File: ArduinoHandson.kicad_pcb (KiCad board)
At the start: 2 copper layers, 33 x 64.4 mm, 19 parts, among them IC1 ATMEGA328-P, P2 USB micro, P3 Power, P4 Digital2, P5 Analog, P6 Digital1, SW1 SW_PUSH, U1 FT232RL, X1 CRYSTAL

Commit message: 配線のみ
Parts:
- turned U1 to 270 degrees
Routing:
- net GND: track 0.00 -> 149.0 mm, vias 0 -> 5
- net +5V: track 0.00 -> 88.4 mm
- net /D13: track 0.00 -> 59.8 mm
- net /D1: track 0.00 -> 36.6 mm
- net /Reset: track 0.00 -> 35.7 mm
- net /D0: track 0.00 -> 34.2 mm
- net +3V3: track 0.00 -> 31.9 mm, vias 0 -> 3
- net /D2: track 0.00 -> 22.7 mm
- net /D4: track 0.00 -> 22.4 mm
- net /D3: track 0.00 -> 22.0 mm
- net Net-(D2-Pad1): track 0.00 -> 19.4 mm, vias 0 -> 1
- net /D8: track 0.00 -> 19.0 mm
- net Net-(D1-Pad1): track 0.00 -> 13.3 mm
- net /D5: track 0.00 -> 12.5 mm
- net /D6: track 0.00 -> 12.5 mm
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
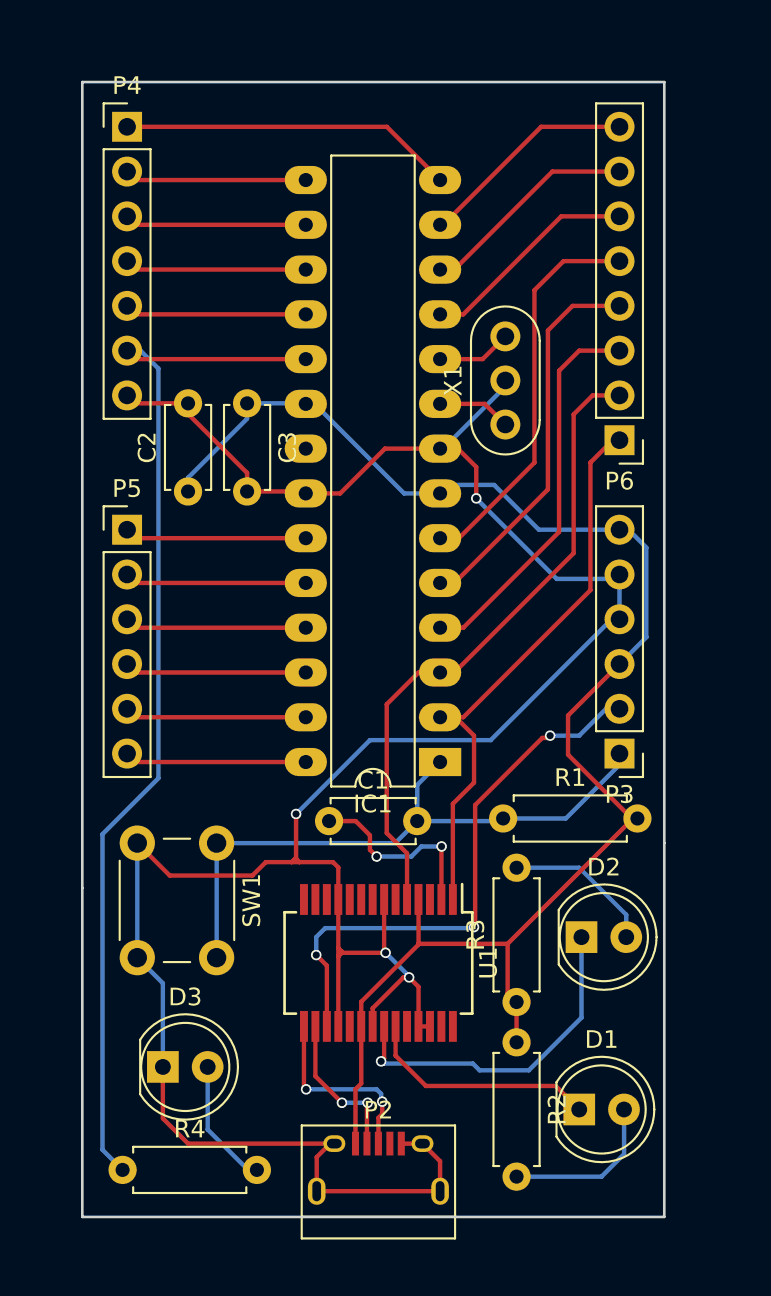
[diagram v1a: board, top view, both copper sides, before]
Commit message: 外形変更、文字表示対応
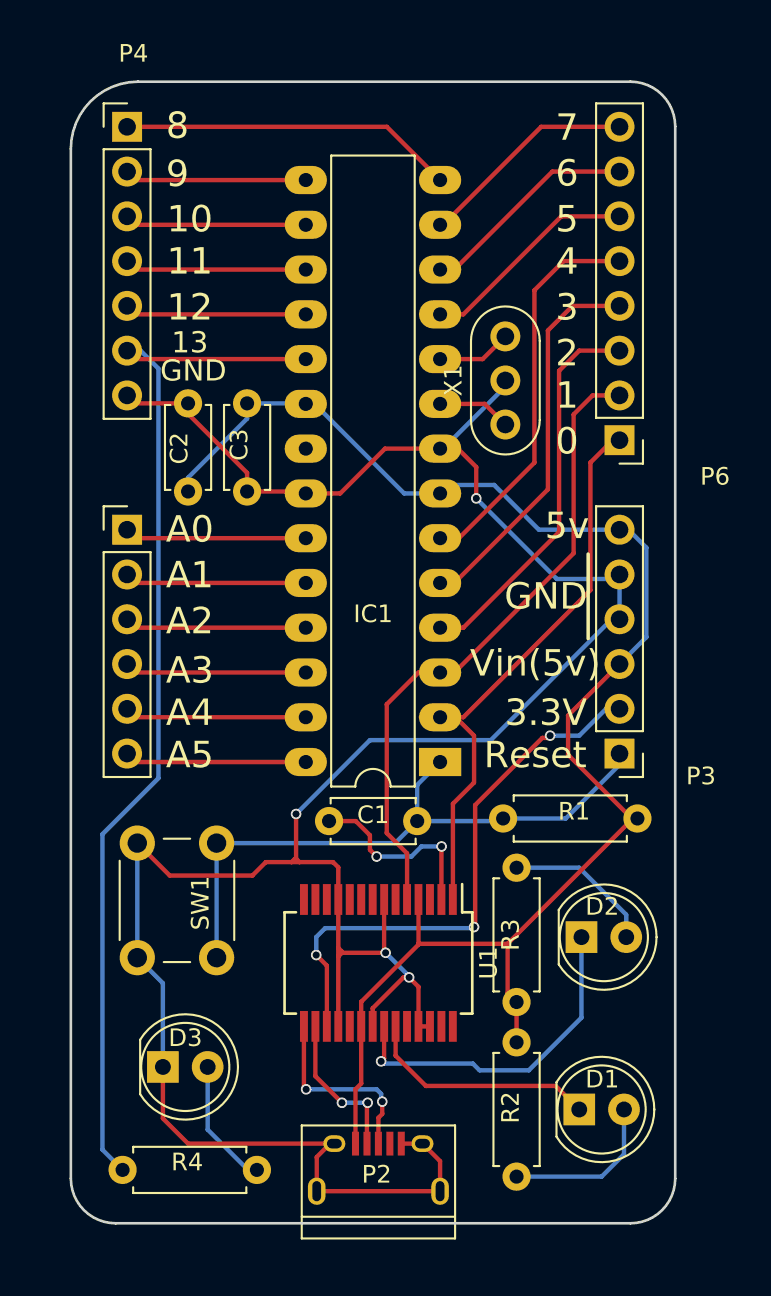
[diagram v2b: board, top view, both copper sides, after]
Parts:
- SW1: value SW_PUSH -> Reset
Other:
- board size 33 x 64.4 mm -> 34.3 x 64.8 mm
- board text added: "0"
- board text added: "1"
- board text added: "10"
- board text added: "11"
- board text added: "12"
- board text added: "13"
- board text added: "2"
- board text added: "3"
- board text added: "3.3V"
- board text added: "4"
- board text added: "5"
- board text added: "5v"
- board text added: "6"
- board text added: "7"
- board text added: "8"
- board text added: "9"
- board text added: "A0"
- board text added: "A1"
- board text added: "A2"
- board text added: "A3"
- board text added: "A4"
- board text added: "A5"
- board text added: "GND"
- board text added: "Reset"
- board text added: "Vin(5v)"

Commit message: ベタグランド
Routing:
- added copper zone on B.Cu, net GND
- added copper zone on F.Cu, net GND

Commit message: 回路図+配線図完成
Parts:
- removed the P2 at (54.9, 94.6)
- added P1: USB_B, Connect:USB_B_MUSB_Straight, F.Cu at (56.2, 90.6)
- SW1: value Reset -> SW_PUSH
- moved R1 24.3 mm to (38.9, 82.4)
- moved D3 23.8 mm to (66.0, 93.8)
- moved R3 16.6 mm to (46.5, 88.8), turned to 180 degrees
- moved R2 16.3 mm to (46.5, 85.6), turned to 180 degrees
- moved D1 11.5 mm to (66.0, 79.8)
- moved R4 6.70 mm to (46.5, 92.0), turned to 180 degrees
- moved SW1 5.72 mm to (40.2, 74.7), turned to 0 degrees
- moved D2 5.28 mm to (66.0, 86.8)
- moved U1 1.33 mm to (54.6, 81.7)
- renumbered P3 to P2, P4 to P3, P5 to P4, P6 to P5
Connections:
- IC1 pad 21: Net-(IC1-Pad21) -> +5V
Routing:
- net Net-(D1-Pad2): track 9.16 -> 34.9 mm
- net Net-(D3-Pad2): track 7.30 -> 32.4 mm
- net Net-(D2-Pad2): track 8.60 -> 31.6 mm
- net GND: track 149.0 -> 129.8 mm, vias 5 -> 3
- net +5V: track 88.4 -> 96.3 mm, vias 0 -> 1
- net /Reset: track 35.7 -> 42.1 mm
- net Net-(D2-Pad1): track 19.4 -> 13.9 mm, vias 1 -> 0
- net Net-(C1-Pad1): track 11.0 -> 8.60 mm, vias 2 -> 1
- net /D-: track 8.75 -> 6.41 mm, vias 2 -> 0
- net Net-(D1-Pad1): track 13.3 -> 15.6 mm
- net +3V3: track 31.9 -> 29.9 mm, vias 3 -> 2
- net /D0: track 34.2 -> 35.8 mm
- net /D+: track 10.9 -> 9.43 mm, vias 2 -> 0
- net /D1: track 36.6 -> 35.3 mm
- net /D13: track 59.8 -> 59.0 mm, vias 0 -> 1
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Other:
- board size 34.3 x 64.8 mm -> 35 x 66 mm
- net class Power added: clearance 0.2, trace_width 0.4, via_dia 0.6, via_drill 0.4

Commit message: 配線図開始
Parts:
- removed D3: 13LED, LEDs:LED_D5.0mm
- removed R4: 500, Resistors_ThroughHole:R_Axial_DIN0207_L6.3mm_D2.5mm_P7.62mm_Horizontal
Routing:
- net /D13: track 59.0 -> 11.7 mm, vias 1 -> 0
- net Net-(D3-Pad2): track 32.4 -> 0.00 mm
- net /A5: track 10.3 -> 0.68 mm
- net /A4: track 10.3 -> 0.68 mm
- net /A3: track 10.3 -> 0.68 mm
- net /A2: track 10.3 -> 0.68 mm
- net /A1: track 10.3 -> 0.68 mm
- net /A0: track 10.3 -> 0.68 mm
- net GND: track 129.8 -> 124.8 mm
